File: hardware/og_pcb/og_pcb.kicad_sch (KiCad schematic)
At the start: 0 parts

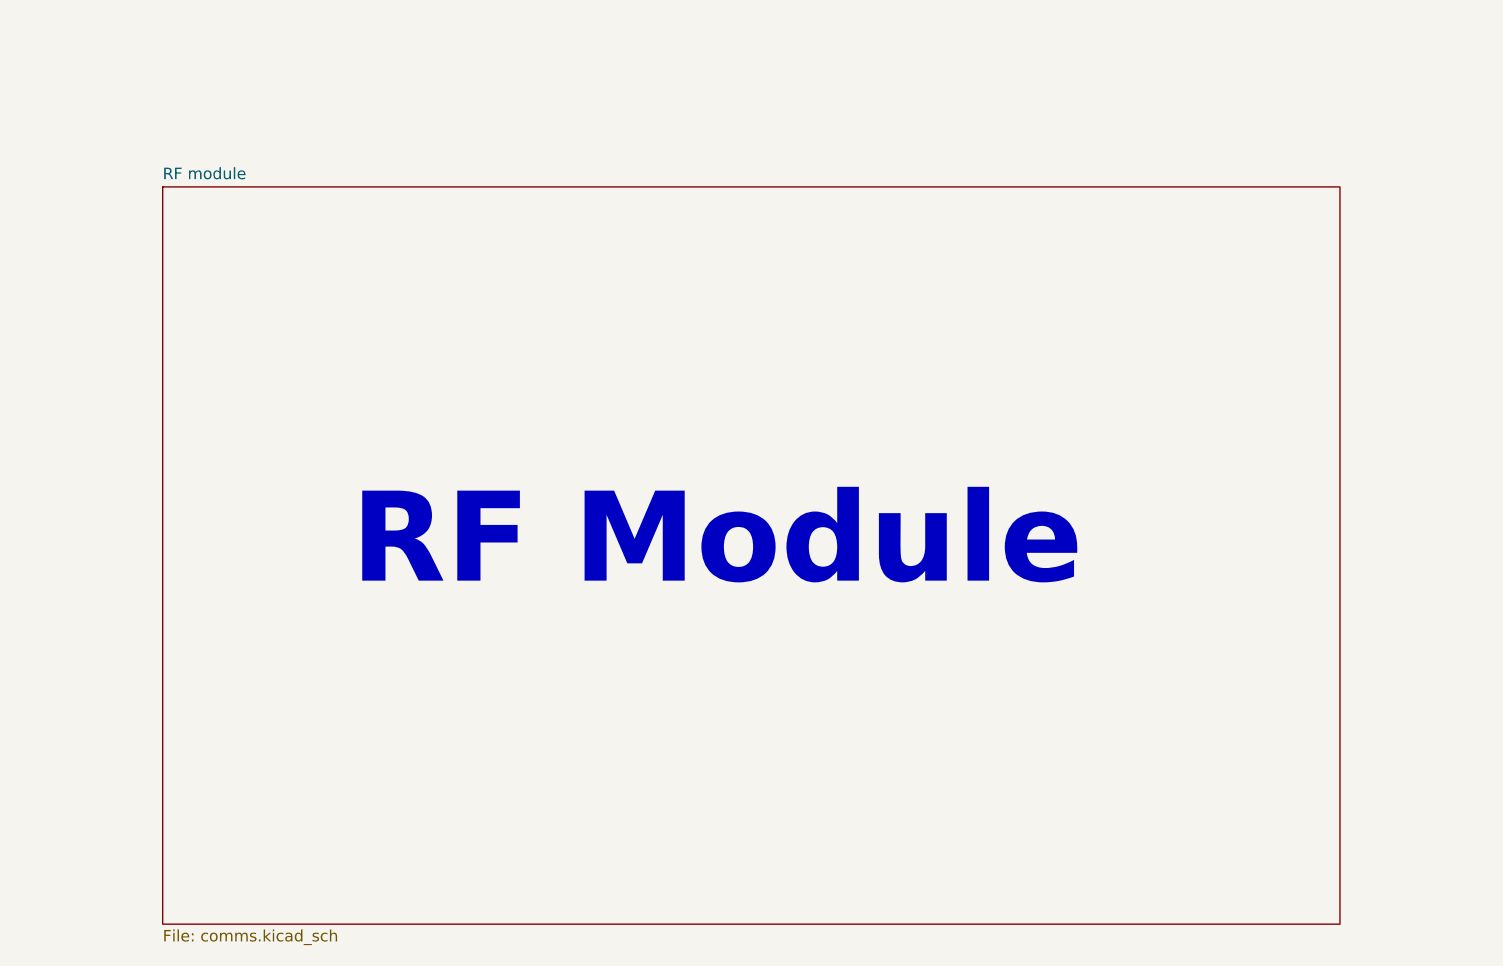
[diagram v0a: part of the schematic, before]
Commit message: updated pcb v2 progress
reimplemented spi microSD, changed power monitor to model with internal shunt resistor, changed power supply from usbc to barrel jack, reconnected vbus to microusb, modified spi and i2c connections (2 i2c connections, 2 spi connections), removed RF module & IMU.

to do:
- find/create footprints for new parts
- verify implementation by reviewing datasheets again
- implement coax connector for analog connection to cosmic watch
- implement gps receiver (must do more research; implement one well-known/documented/used b4)
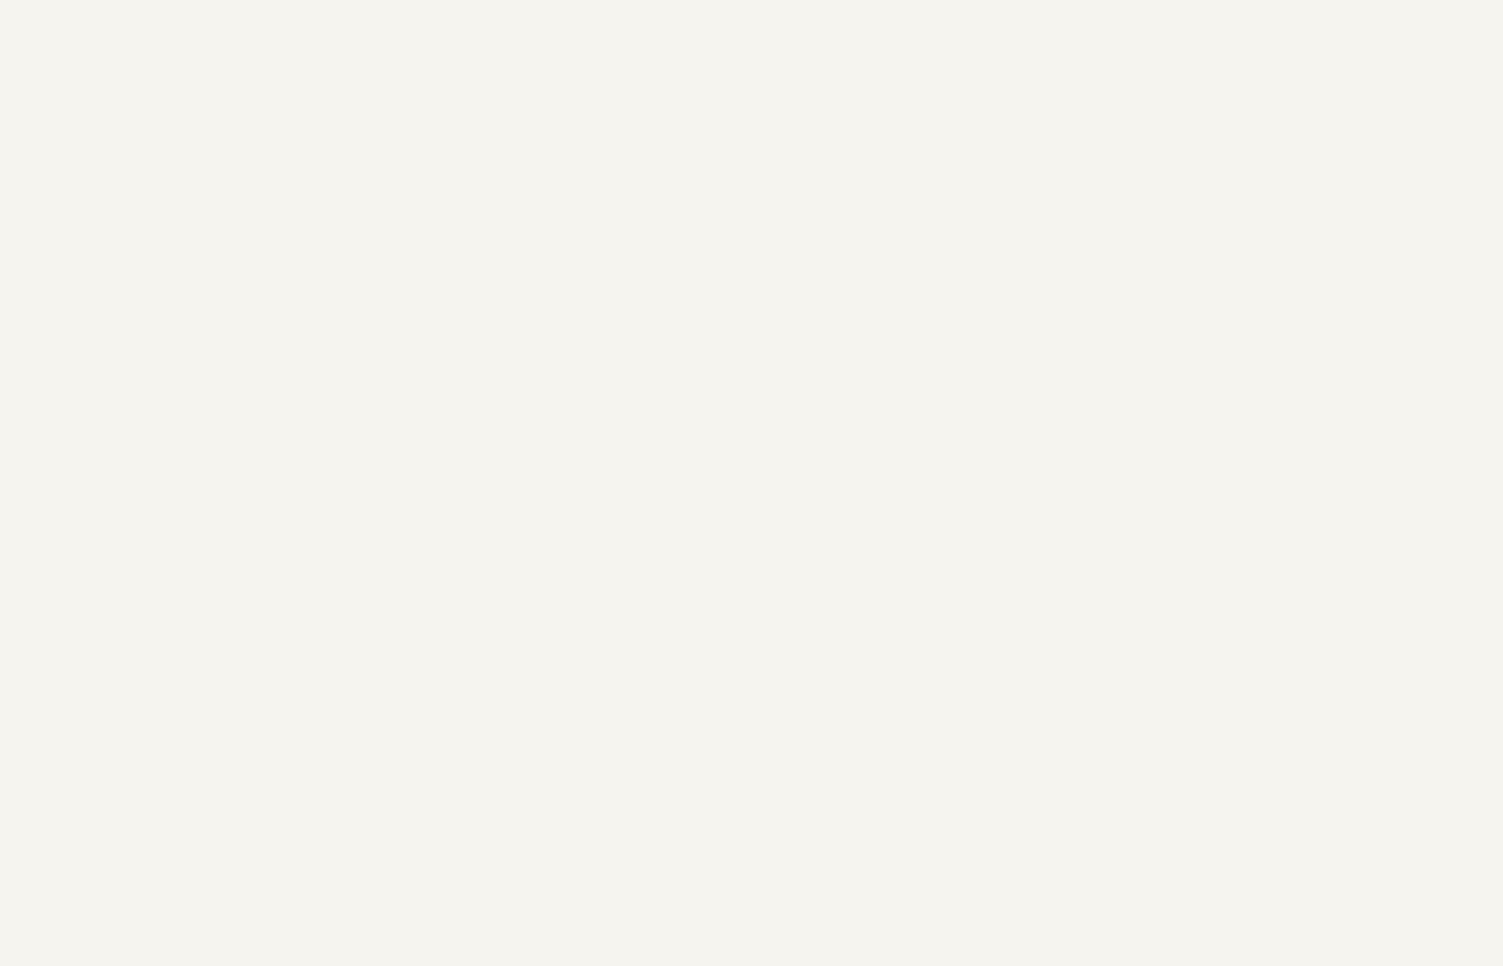
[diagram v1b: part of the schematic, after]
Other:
- removed sheet RF module
- note removed: "RF Module"
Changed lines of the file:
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@@
-		)
-	)
-	(text "RF Module"
-		(exclude_from_sim no)
-		(at 193.04 331.47 0)
-		(effects
-			(font
-				(size 10 10)
-				(thickness 2)
-				(bold yes)
-			)
 		)
 	)
@@
 				)
 			)
-		)
-	)
-	(sheet
-		(at 131.445 292.1)
-		(size 130.81 81.915)
-		(exclude_from_sim no)
-		(in_bom yes)
-		(on_board yes)
-		(dnp no)
-		(fields_autoplaced yes)
-		(stroke
-			(width 0.1524)
-			(type solid)
-		)
-		(fill
-			(color 0 0 0 0.0000)
-		)
-		(property "Sheetname" "RF module"
-			(at 131.445 291.3884 0)
-			(effects
-				(font
-					(size 1.27 1.27)
-				)
-				(justify left bottom)
-			)
-		)
-		(property "Sheetfile" "comms.kicad_sch"
-			(at 131.445 374.5996 0)
-			(effects
-				(font
-					(size 1.27 1.27)
-				)
-				(justify left top)
-			)
-		)
-		(instances
-			(project "og_pcb"
-				(path "/e4ef350a-b140-44e0-8bc3-973fc24bf90a"
-					(page "5")
-				)
-			)
